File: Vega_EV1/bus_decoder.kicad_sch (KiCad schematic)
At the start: 21 parts, among them U14 74AHCT00, U15 74AHCT02, U16 74AHCT04, U17 74AHCT02, U18 74AHCT32, U19 74AHCT20, U20 74AHCT20, U21 74AHCT138, U4 74AHCT10

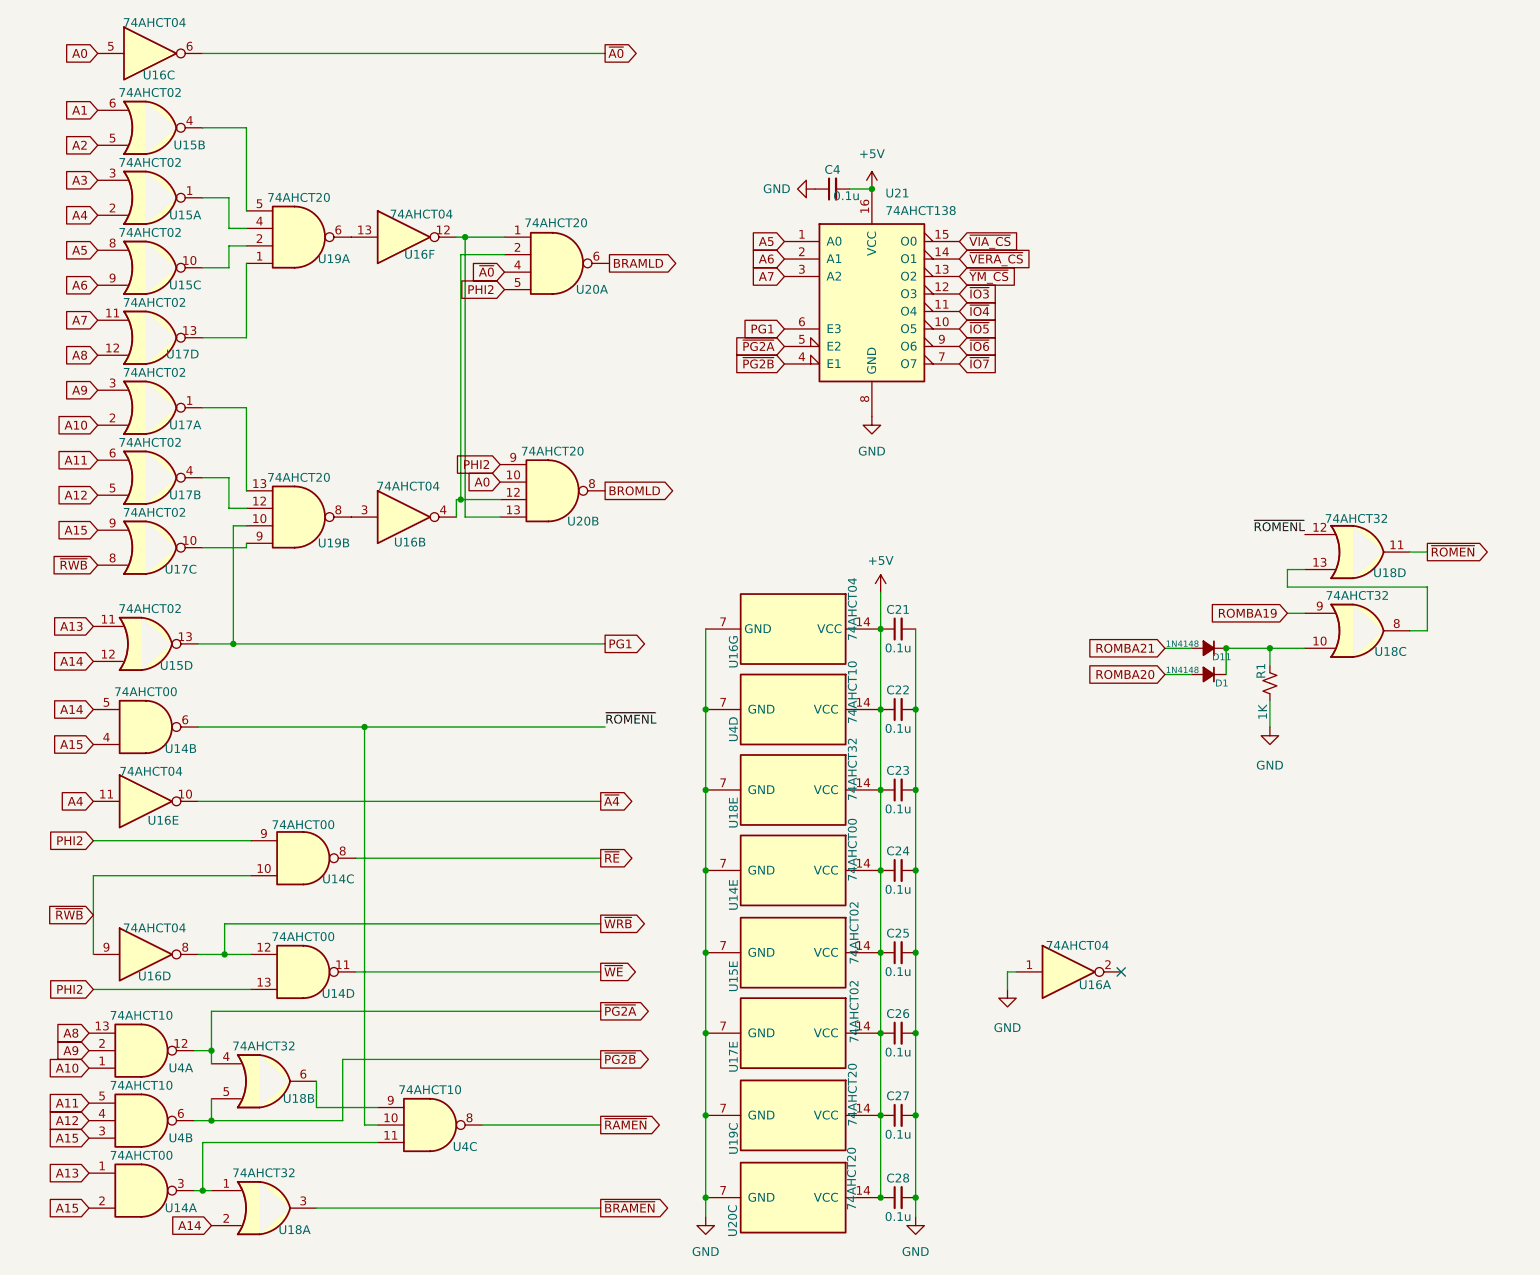
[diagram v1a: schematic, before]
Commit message: More space between Edge and YM2151 Add IEC logic back in IDC headers for NES and IEC
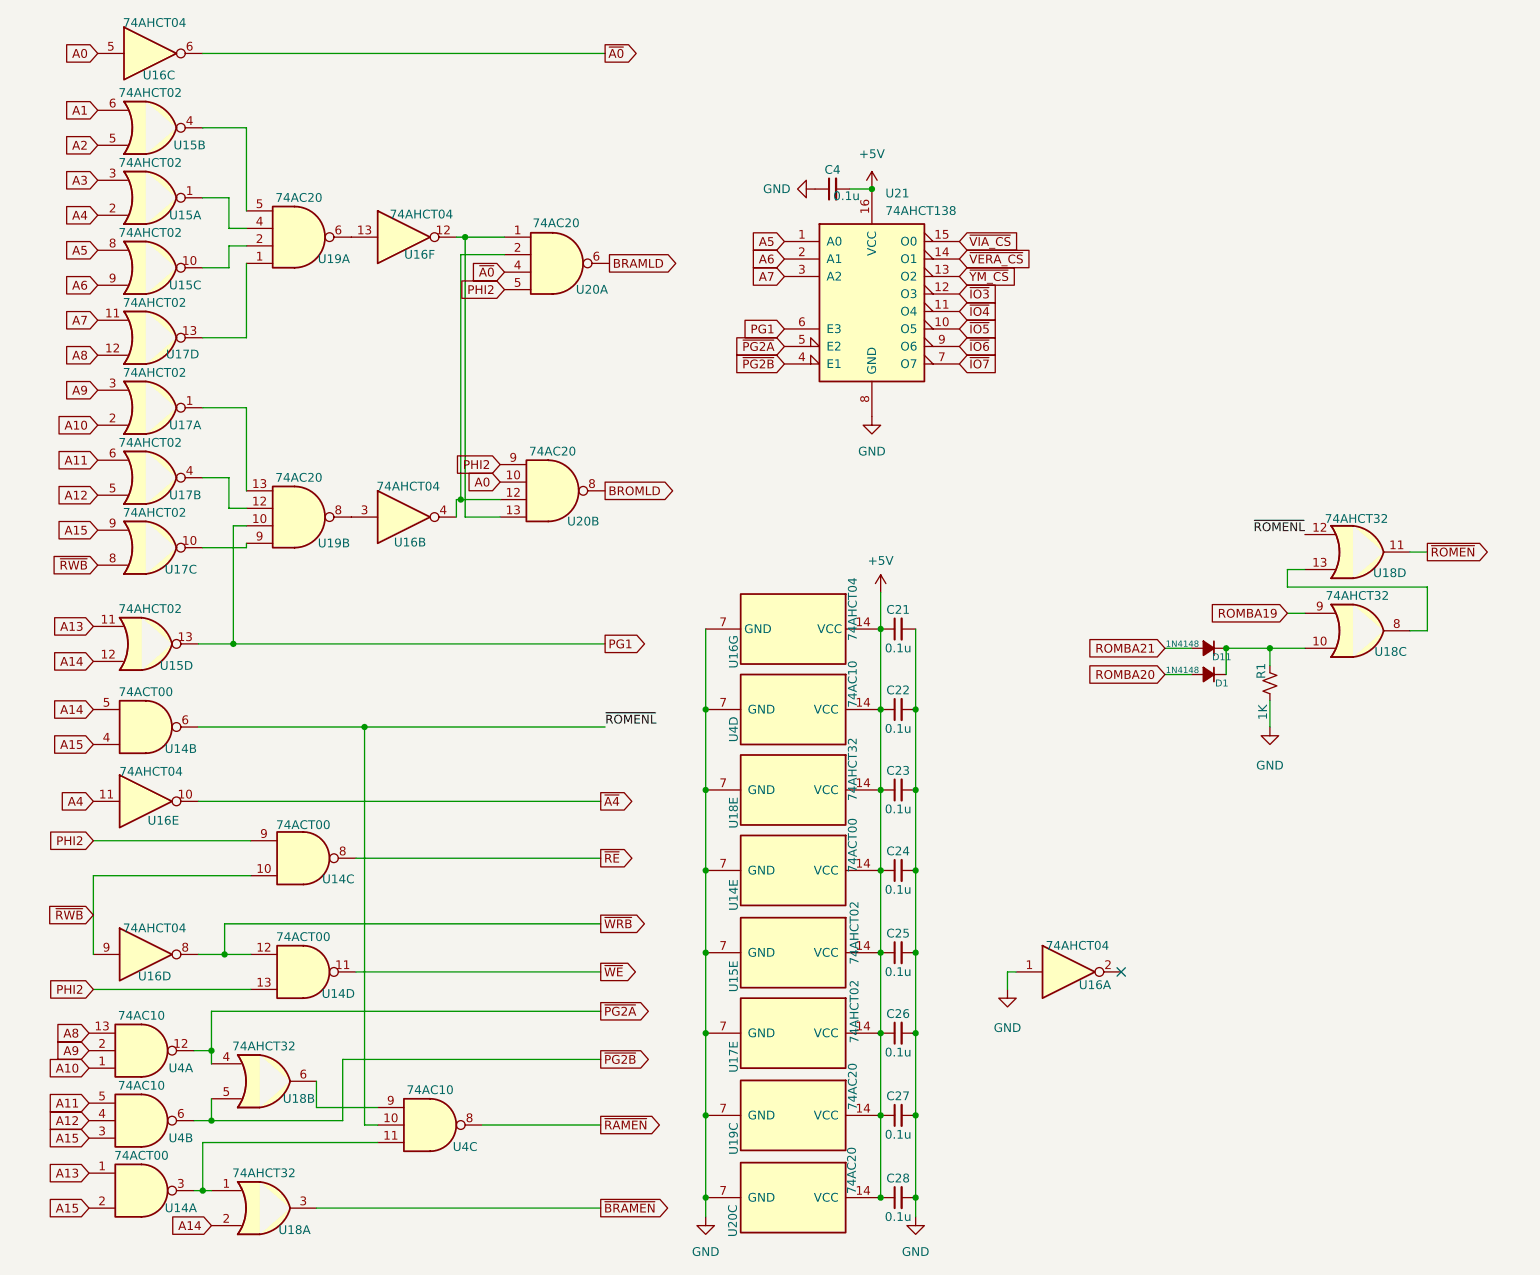
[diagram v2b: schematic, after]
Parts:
- U14: value 74AHCT00 -> 74ACT00
- U19, U20: value 74AHCT20 -> 74AC20
- U4: value 74AHCT10 -> 74AC10
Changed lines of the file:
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@@
 	(label "~{ROMENL}"
 		(at 203.2 90.17 180)
-		(fields_autoplaced yes)
 		(effects
 			(font
@@
 	(label "~{ROMENL}"
 		(at 101.6 118.11 0)
-		(fields_autoplaced yes)
 		(effects
 			(font
@@
 			)
 		)
-		(property "Value" "74AHCT10"
+		(property "Value" "74AC10"
 			(at 34.29 160.02 0)
 			(effects
@@
 			)
 		)
-		(property "Value" "74AHCT20"
+		(property "Value" "74AC20"
 			(at 57.15 81.915 0)
 			(effects
@@
 			)
 		)
-		(property "Value" "74AHCT20"
+		(property "Value" "74AC20"
 			(at 93.98 78.105 0)
 			(effects
@@
 			)
 		)
-		(property "Value" "74AHCT00"
+		(property "Value" "74ACT00"
 			(at 34.29 180.34 0)
 			(effects
@@
 			)
 		)
-		(property "Value" "74AHCT10"
+		(property "Value" "74AC10"
 			(at 34.29 170.18 0)
 			(effects
@@
 			)
 		)
-		(property "Value" "74AHCT20"
+		(property "Value" "74AC20"
 			(at 137.414 179.07 0)
 			(effects
@@
 			)
 		)
-		(property "Value" "74AHCT10"
+		(property "Value" "74AC10"
 			(at 76.2 170.815 0)
 			(effects
@@
 			)
 		)
-		(property "Value" "74AHCT20"
+		(property "Value" "74AC20"
 			(at 137.541 166.878 0)
 			(effects
@@
 			)
 		)
-		(property "Value" "74AHCT10"
+		(property "Value" "74AC10"
 			(at 137.541 108.458 0)
 			(effects
@@
 			)
 		)
-		(property "Value" "74AHCT00"
+		(property "Value" "74ACT00"
 			(at 34.925 113.03 0)
 			(effects
@@
 			)
 		)
-		(property "Value" "74AHCT20"
+		(property "Value" "74AC20"
 			(at 57.15 41.275 0)
 			(effects
@@
 			)
 		)
-		(property "Value" "74AHCT00"
+		(property "Value" "74ACT00"
 			(at 137.541 131.318 0)
 			(effects
@@
 			)
 		)
-		(property "Value" "74AHCT00"
+		(property "Value" "74ACT00"
 			(at 57.785 148.59 0)
 			(effects
@@
 			)
 		)
-		(property "Value" "74AHCT00"
+		(property "Value" "74ACT00"
 			(at 57.785 132.334 0)
 			(effects
@@
 			)
 		)
-		(property "Value" "74AHCT20"
+		(property "Value" "74AC20"
 			(at 94.488 44.958 0)
 			(effects
